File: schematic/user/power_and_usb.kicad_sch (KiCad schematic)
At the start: 32 parts, among them J1 TYPE-C-31-M-04, Q1 AO3401A, Q2 AO3401A, Q5 MBT3904DW1T1, U1 TP4056, U2 MAX17048G+T10, U3 NCP167AFCT330T2G, U6 ESD122DMXR

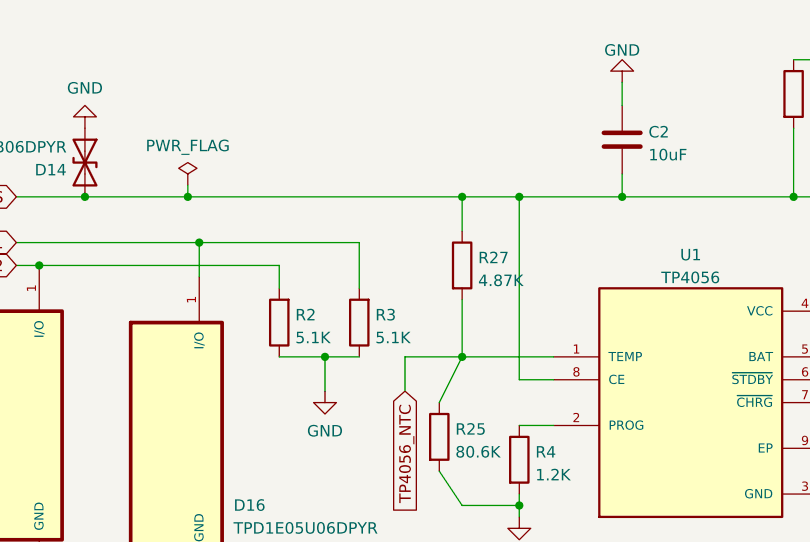
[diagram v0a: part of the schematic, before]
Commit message: v0.7 board: add time delay for TP4056 to avoid violating USB inrush spec.
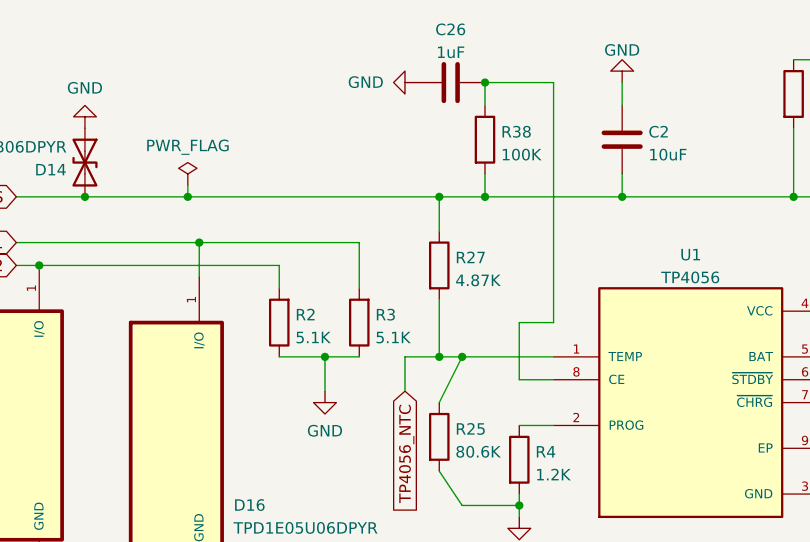
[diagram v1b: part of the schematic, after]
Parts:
- added C26: 1uF, Capacitor_SMD:C_0402_1005Metric, symbol Device:C
- added R38: 100K, Resistor_SMD:R_0402_1005Metric, symbol Device:R
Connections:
- net GND: now also C26.1
- net USBC_VBUS: now also R38.2; no longer U1.8 (CE)
- new net: C26.2, R38.1, U1.8 (CE)
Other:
- moved on the sheet: R27
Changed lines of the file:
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@@
   (junction (at 166.37 35.56) (diameter 0) (color 0 0 0 0)
   )
+  (junction (at 101.6 35.56) (diameter 0) (color 0 0 0 0)
+  )
   (junction (at 241.3 57.15) (diameter 0) (color 0 0 0 0)
   )
@@
   (junction (at 252.73 45.72) (diameter 0) (color 0 0 0 0)
   )
+  (junction (at 101.6 22.86) (diameter 0) (color 0 0 0 0)
+  )
   (junction (at 180.34 35.56) (diameter 0) (color 0 0 0 0)
   )
@@
   (junction (at 146.05 68.58) (diameter 0) (color 0 0 0 0)
   )
+  (junction (at 96.52 53.34) (diameter 0) (color 0 0 0 0)
+  )
   (junction (at 106.68 148.59) (diameter 0) (color 0 0 0 0)
   )
-  (junction (at 99.06 35.56) (diameter 0) (color 0 0 0 0)
-  )
   (junction (at 254 144.78) (diameter 0) (color 0 0 0 0)
   )
+  (junction (at 96.52 35.56) (diameter 0) (color 0 0 0 0)
+  )
   (junction (at 153.67 68.58) (diameter 0) (color 0 0 0 0)
   )
@@
   )
   (junction (at 69.85 40.64) (diameter 0) (color 0 0 0 0)
-  )
-  (junction (at 105.41 35.56) (diameter 0) (color 0 0 0 0)
   )
   (junction (at 254 124.46) (diameter 0) (color 0 0 0 0)
@@
     (stroke (width 0) (type default) (color 0 0 0 0))
   )
+  (wire (pts (xy 105.41 49.53) (xy 105.41 55.88))
+    (stroke (width 0) (type default) (color 0 0 0 0))
+  )
   (wire (pts (xy 99.06 69.85) (xy 105.41 69.85))
     (stroke (width 0) (type default) (color 0 0 0 0))
@@
     (stroke (width 0) (type default) (color 0 0 0 0))
   )
+  (wire (pts (xy 101.6 22.86) (xy 101.6 25.4))
+    (stroke (width 0) (type default) (color 0 0 0 0))
+  )
   (wire (pts (xy 135.89 27.94) (xy 135.89 35.56))
     (stroke (width 0) (type default) (color 0 0 0 0))
@@
     (stroke (width 0) (type default) (color 0 0 0 0))
   )
-  (wire (pts (xy 99.06 53.34) (xy 92.71 53.34))
+  (wire (pts (xy 99.06 53.34) (xy 96.52 53.34))
+    (stroke (width 0) (type default) (color 0 0 0 0))
+  )
+  (wire (pts (xy 101.6 22.86) (xy 109.22 22.86))
     (stroke (width 0) (type default) (color 0 0 0 0))
   )
@@
     (stroke (width 0) (type default) (color 0 0 0 0))
   )
+  (wire (pts (xy 109.22 22.86) (xy 109.22 49.53))
+    (stroke (width 0) (type default) (color 0 0 0 0))
+  )
   (wire (pts (xy 148.59 35.56) (xy 166.37 35.56))
     (stroke (width 0) (type default) (color 0 0 0 0))
@@
     (stroke (width 0) (type default) (color 0 0 0 0))
   )
+  (wire (pts (xy 96.52 35.56) (xy 101.6 35.56))
+    (stroke (width 0) (type default) (color 0 0 0 0))
+  )
   (wire (pts (xy 213.36 52.07) (xy 213.36 57.15))
     (stroke (width 0) (type default) (color 0 0 0 0))
@@
     (stroke (width 0) (type default) (color 0 0 0 0))
   )
+  (wire (pts (xy 96.52 53.34) (xy 92.71 53.34))
+    (stroke (width 0) (type default) (color 0 0 0 0))
+  )
   (wire (pts (xy 163.83 82.55) (xy 166.37 82.55))
     (stroke (width 0) (type default) (color 0 0 0 0))
@@
     (stroke (width 0) (type default) (color 0 0 0 0))
   )
-  (wire (pts (xy 105.41 35.56) (xy 116.84 35.56))
-    (stroke (width 0) (type default) (color 0 0 0 0))
-  )
   (polyline (pts (xy 278.13 97.79) (xy 278.13 154.94))
     (stroke (width 0) (type default) (color 0 0 0 0))
@@
     (stroke (width 0) (type default) (color 0 0 0 0))
   )
+  (wire (pts (xy 109.22 49.53) (xy 105.41 49.53))
+    (stroke (width 0) (type default) (color 0 0 0 0))
+  )
   (wire (pts (xy 250.19 119.38) (xy 254 119.38))
     (stroke (width 0) (type default) (color 0 0 0 0))
@@
     (stroke (width 0) (type default) (color 0 0 0 0))
   )
+  (wire (pts (xy 96.52 46.99) (xy 96.52 53.34))
+    (stroke (width 0) (type default) (color 0 0 0 0))
+  )
   (wire (pts (xy 144.78 58.42) (xy 139.7 58.42))
     (stroke (width 0) (type default) (color 0 0 0 0))
@@
     (stroke (width 0) (type default) (color 0 0 0 0))
   )
-  (wire (pts (xy 99.06 46.99) (xy 99.06 53.34))
-    (stroke (width 0) (type default) (color 0 0 0 0))
-  )
   (wire (pts (xy 166.37 27.94) (xy 166.37 35.56))
     (stroke (width 0) (type default) (color 0 0 0 0))
@@
     (stroke (width 0) (type default) (color 0 0 0 0))
   )
+  (wire (pts (xy 101.6 33.02) (xy 101.6 35.56))
+    (stroke (width 0) (type default) (color 0 0 0 0))
+  )
   (wire (pts (xy 252.73 45.72) (xy 260.35 45.72))
     (stroke (width 0) (type default) (color 0 0 0 0))
@@
     (stroke (width 0) (type default) (color 0 0 0 0))
   )
-  (wire (pts (xy 68.58 35.56) (xy 99.06 35.56))
+  (wire (pts (xy 68.58 35.56) (xy 96.52 35.56))
     (stroke (width 0) (type default) (color 0 0 0 0))
   )
@@
     (stroke (width 0) (type default) (color 0 0 0 0))
   )
-  (wire (pts (xy 99.06 35.56) (xy 99.06 39.37))
-    (stroke (width 0) (type default) (color 0 0 0 0))
-  )
-  (wire (pts (xy 99.06 35.56) (xy 105.41 35.56))
-    (stroke (width 0) (type default) (color 0 0 0 0))
-  )
   (wire (pts (xy 69.85 40.64) (xy 69.85 44.45))
     (stroke (width 0) (type default) (color 0 0 0 0))
@@
     (stroke (width 0) (type default) (color 0 0 0 0))
   )
+  (wire (pts (xy 96.52 35.56) (xy 96.52 39.37))
+    (stroke (width 0) (type default) (color 0 0 0 0))
+  )
   (wire (pts (xy 153.67 53.34) (xy 166.37 53.34))
     (stroke (width 0) (type default) (color 0 0 0 0))
@@
     (stroke (width 0) (type default) (color 0 0 0 0))
   )
+  (wire (pts (xy 101.6 35.56) (xy 116.84 35.56))
+    (stroke (width 0) (type default) (color 0 0 0 0))
+  )
   (wire (pts (xy 57.15 35.56) (xy 68.58 35.56))
-    (stroke (width 0) (type default) (color 0 0 0 0))
-  )
-  (wire (pts (xy 105.41 55.88) (xy 105.41 35.56))
     (stroke (width 0) (type default) (color 0 0 0 0))
   )
@@
     )
     (property "LCSC" "C2286" (id 4) (at 154.94 24.13 0)
+      (effects (font (size 1.27 1.27)) hide)
+    )
+    (pin "1")
+    (pin "2")
+  )
+  (symbol (lib_id "Device:R") (at 101.6 29.21 0) (unit 1)
+    (in_bom yes) (on_board yes) (fields_autoplaced)
+    (property "Reference" "R38" (id 0) (at 103.378 28.3753 0)
+      (effects (font (size 1.27 1.27)) (justify left))
+    )
+    (property "Value" "100K" (id 1) (at 103.378 30.9122 0)
+      (effects (font (size 1.27 1.27)) (justify left))
+    )
+    (property "Footprint" "Resistor_SMD:R_0402_1005Metric" (id 2) (at 99.822 29.21 90)
+      (effects (font (size 1.27 1.27)) hide)
+    )
+    (property "Datasheet" "https://datasheet.lcsc.com/lcsc/2206010100_UNI-ROYAL-Uniroyal-Elec-0402WGF1003TCE_C25741.pdf" (id 3) (at 101.6 29.21 0)
+      (effects (font (size 1.27 1.27)) hide)
+    )
+    (property "LCSC" "C25741" (id 4) (at 101.6 29.21 0)
       (effects (font (size 1.27 1.27)) hide)
     )
@@
     )
     (pin "1")
+  )
+  (symbol (lib_id "Device:C") (at 97.79 22.86 90) (unit 1)
+    (in_bom yes) (on_board yes) (fields_autoplaced)
+    (property "Reference" "C26" (id 0) (at 97.79 17.0012 90))
+    (property "Value" "1uF" (id 1) (at 97.79 19.5381 90))
+    (property "Footprint" "Capacitor_SMD:C_0402_1005Metric" (id 2) (at 101.6 21.8948 0)
+      (effects (font (size 1.27 1.27)) hide)
+    )
+    (property "Datasheet" "https://datasheet.lcsc.com/lcsc/1810191214_Samsung-Electro-Mechanics-CL05A105KP5NNNC_C14445.pdf" (id 3) (at 97.79 22.86 0)
+      (effects (font (size 1.27 1.27)) hide)
+    )
+    (property "LCSC" "C14445" (id 4) (at 97.79 22.86 0)
+      (effects (font (size 1.27 1.27)) hide)
+    )
+    (pin "1")
+    (pin "2")
   )
   (symbol (lib_id "Device:R") (at 106.68 156.21 0) (unit 1)
@@
     (pin "S8")
   )
+  (symbol (lib_id "power:GND") (at 93.98 22.86 270) (unit 1)
+    (in_bom yes) (on_board yes)
+    (property "Reference" "#PWR054" (id 0) (at 87.63 22.86 0)
+      (effects (font (size 1.27 1.27)) hide)
+    )
+    (property "Value" "GND" (id 1) (at 86.36 22.86 90)
+      (effects (font (size 1.27 1.27)) (justify left))
+    )
+    (property "Footprint" "" (id 2) (at 93.98 22.86 0)
+      (effects (font (size 1.27 1.27)) hide)
+    )
+    (property "Datasheet" "" (id 3) (at 93.98 22.86 0)
+      (effects (font (size 1.27 1.27)) hide)
+    )
+    (pin "1")
+  )
   (symbol (lib_id "Device:Thermistor_NTC") (at 166.37 76.2 0) (unit 1)
     (in_bom yes) (on_board yes) (fields_autoplaced)
@@
     (pin "2")
   )
-  (symbol (lib_id "Device:R") (at 99.06 43.18 0) (unit 1)
-    (in_bom yes) (on_board yes) (fields_autoplaced)
-    (property "Reference" "R27" (id 0) (at 100.838 42.3453 0)
-      (effects (font (size 1.27 1.27)) (justify left))
-    )
-    (property "Value" "4.87K" (id 1) (at 100.838 44.8822 0)
-      (effects (font (size 1.27 1.27)) (justify left))
-    )
-    (property "Footprint" "Resistor_SMD:R_0805_2012Metric" (id 2) (at 97.282 43.18 90)
-      (effects (font (size 1.27 1.27)) hide)
-    )
-    (property "Datasheet" "https://datasheet.lcsc.com/lcsc/1810261826_Viking-Tech-ARG05FTC4871_C218605.pdf" (id 3) (at 99.06 43.18 0)
-      (effects (font (size 1.27 1.27)) hide)
-    )
-    (property "LCSC" "C218605" (id 4) (at 99.06 43.18 0)
-      (effects (font (size 1.27 1.27)) hide)
-    )
+  (symbol (lib_id "Device:R") (at 96.52 43.18 0) (unit 1)
+    (in_bom yes) (on_board yes) (fields_autoplaced)
+    (property "Reference" "R27" (id 0) (at 98.298 42.3453 0)
+      (effects (font (size 1.27 1.27)) (justify left))
+    )
+    (property "Value" "4.87K" (id 1) (at 98.298 44.8822 0)
+      (effects (font (size 1.27 1.27)) (justify left))
+    )
+    (property "Footprint" "Resistor_SMD:R_0805_2012Metric" (id 2) (at 94.742 43.18 90)
+      (effects (font (size 1.27 1.27)) hide)
+    )
+    (property "Datasheet" "https://datasheet.lcsc.com/lcsc/1810261826_Viking-Tech-ARG05FTC4871_C218605.pdf" (id 3) (at 96.52 43.18 0)
+      (effects (font (size 1.27 1.27)) hide)
+    )
+    (property "LCSC" "C218605" (id 4) (at 96.52 43.18 0)
+      (effects (font (size 1.27 1.27)) hide)
+    )

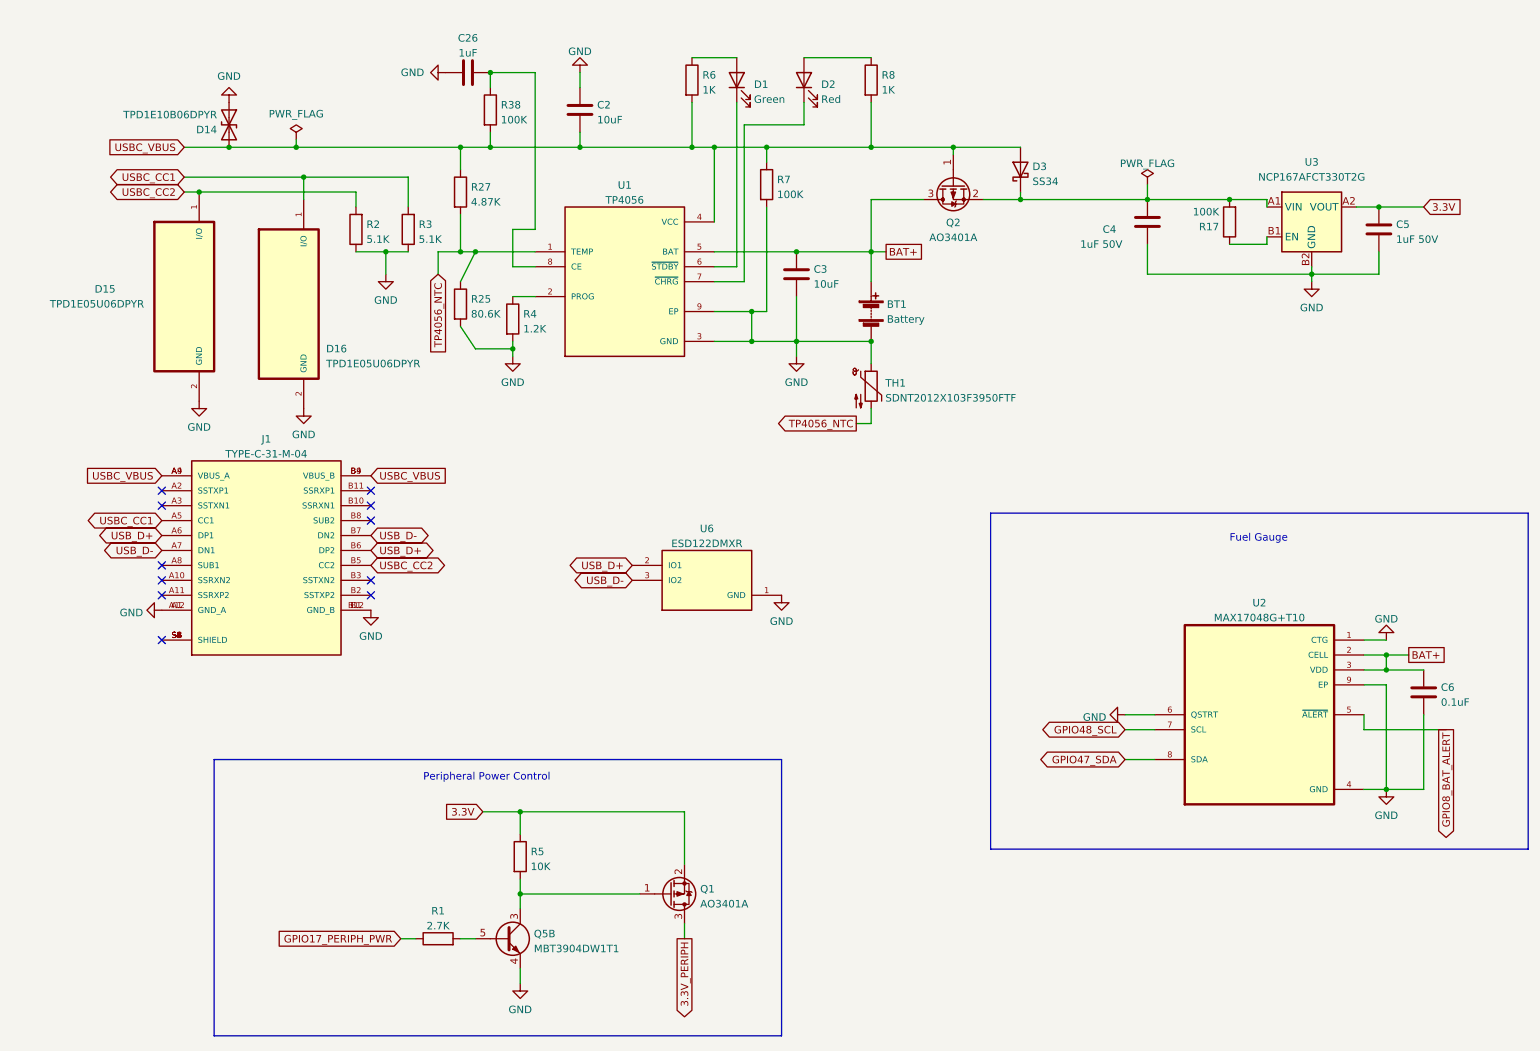
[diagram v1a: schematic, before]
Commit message: v0.7 board: add pi filter for USBC_VBUS to reduce noise coupling into rest of system.
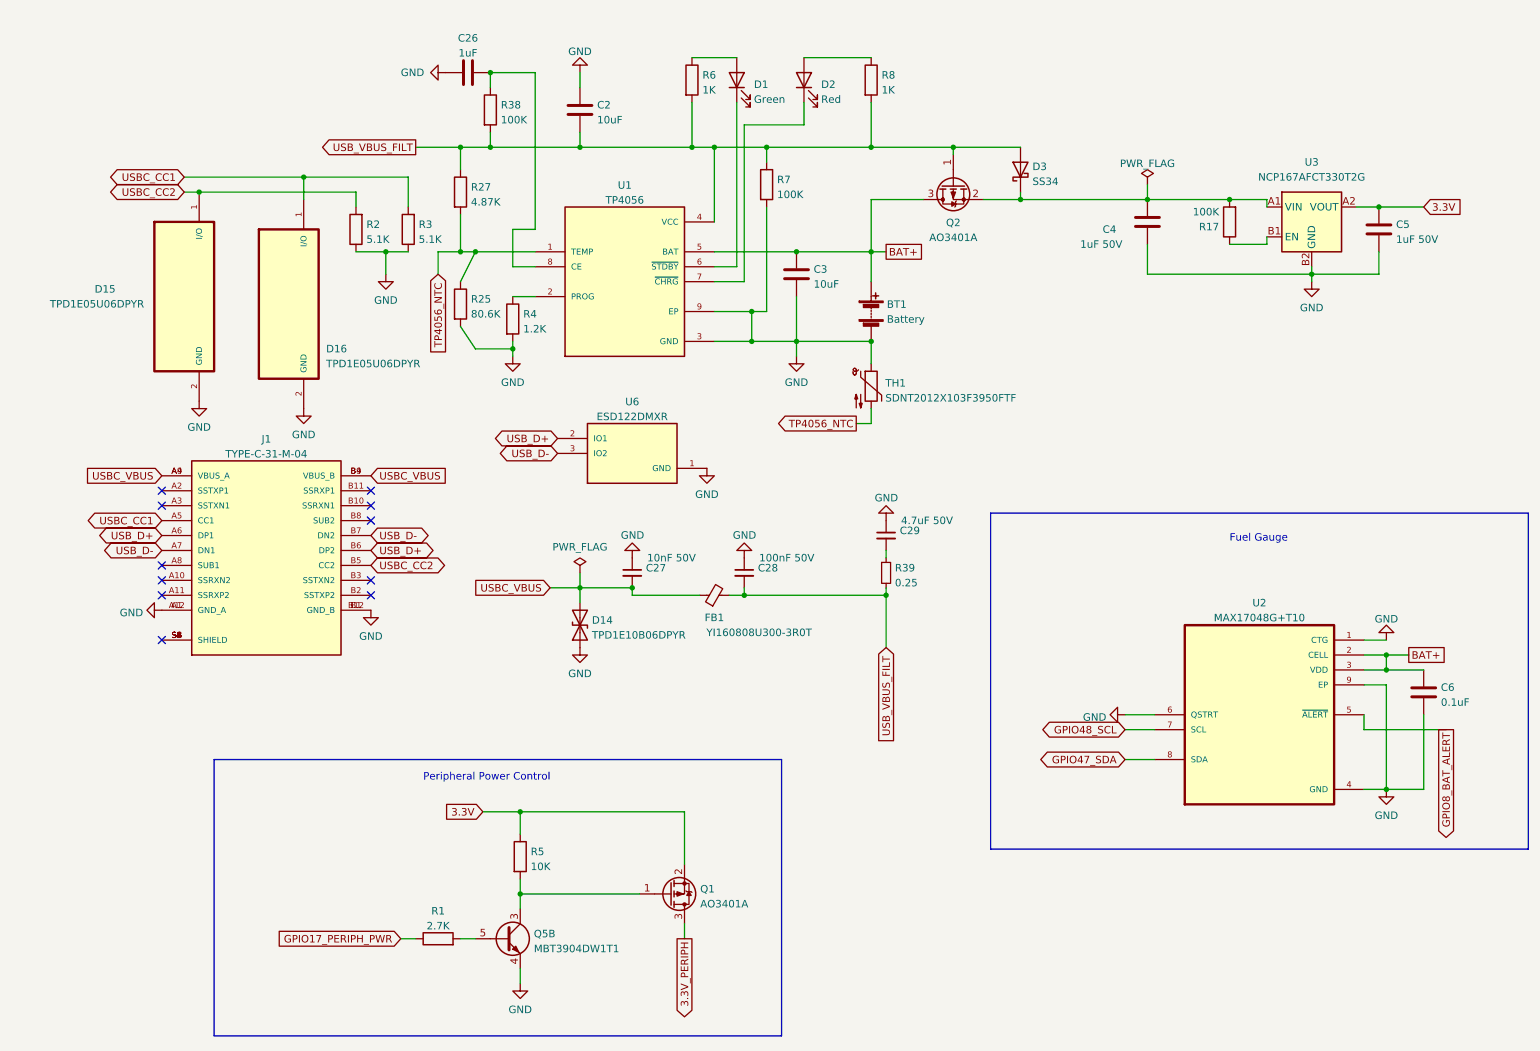
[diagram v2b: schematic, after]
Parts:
- added C27: 10nF 50V, Capacitor_SMD:C_0402_1005Metric, symbol Device:C_Small
- added C28: 100nF 50V, Capacitor_SMD:C_0402_1005Metric, symbol Device:C_Small
- added C29: 4.7uF 50V, Capacitor_SMD:C_0805_2012Metric, symbol Device:C_Small
- added FB1: YI160808U300-3R0T, Inductor_SMD:L_0603_1608Metric, symbol Device:FerriteBead_Small
- added R39: 0.25, Resistor_SMD:R_0603_1608Metric, symbol Device:R_Small
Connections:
- net GND: now also C27.1, C28.1, C29.1
- net USBC_VBUS: now also C27.2, FB1.1; no longer C2.2, D3.2 (A), Q2.1 (G), R27.1, R38.2, R6.2, R7.1, R8.2, U1.4 (VCC)
- new net: C29.2, R39.1
- new net USB_VBUS_FILT: C2.2, C28.2, D3.2 (A), FB1.2, Q2.1 (G), R27.1, R38.2, R39.2, R6.2, R7.1, R8.2, U1.4 (VCC)
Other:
- moved on the sheet: D14, U6
